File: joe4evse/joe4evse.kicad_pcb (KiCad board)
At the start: 2 copper layers, 100 x 100 mm, 77 parts, among them J1 USB_B_Micro, J10 Conn_01x02, J11 Conn_01x02, J2 Conn_01x03, J3 Conn_01x03, J4 Conn_01x02, J5 Conn_01x03, J6 CONNFLY_Elec_DS1129-04-S8B0P-X, J7 8P8C_LED_Shielded, J8 Conn_01x02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

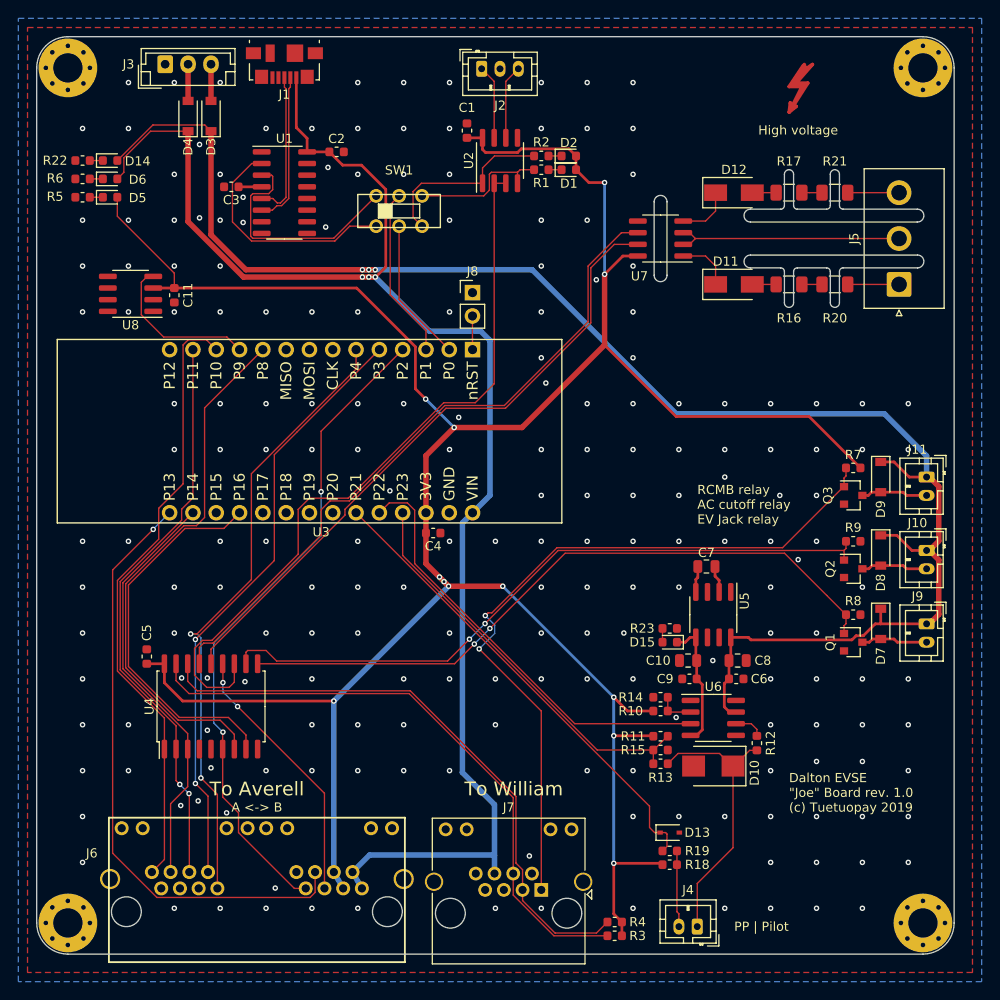
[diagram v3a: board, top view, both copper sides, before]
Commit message: joe/*: Add 0.1" header for easy access to RJ45 signals
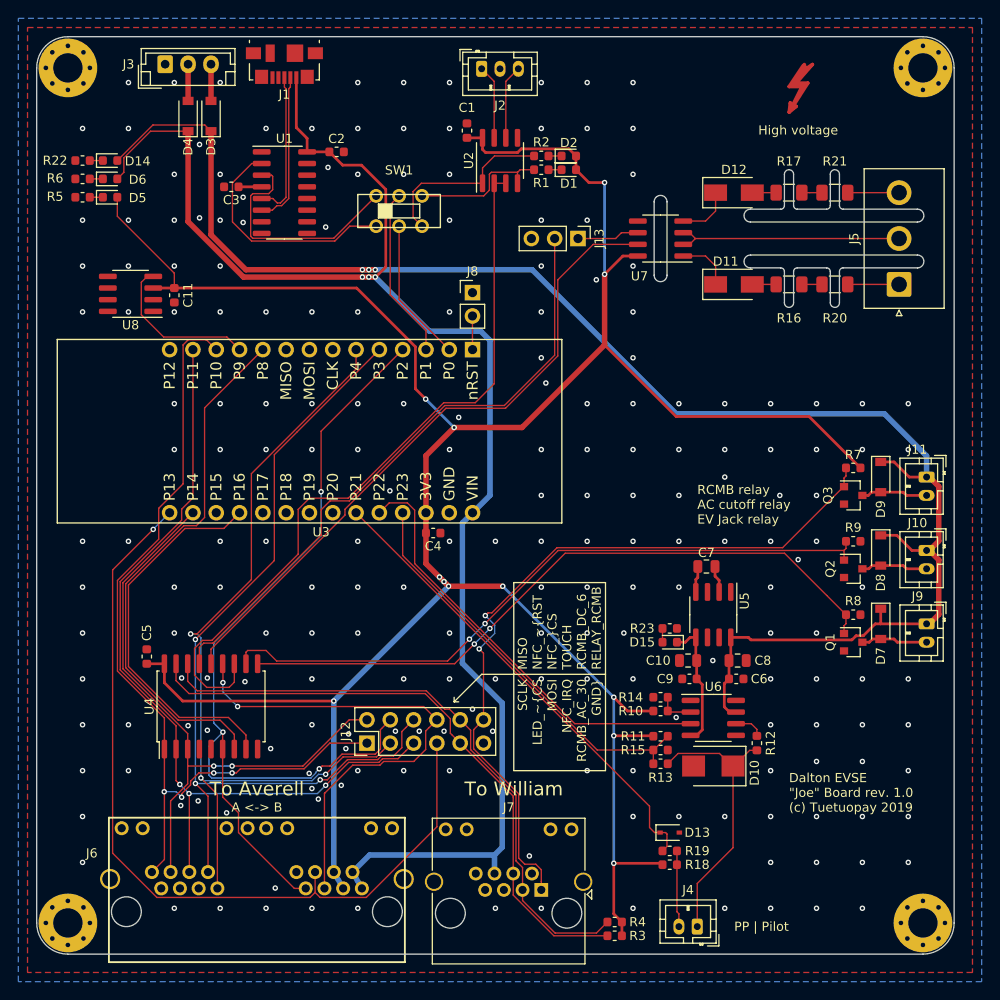
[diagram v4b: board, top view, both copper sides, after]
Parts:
- added J12: Conn_02x06_Odd_Even, Connector_PinHeader_2.54mm:PinHeader_2x06_P2.54mm_Vertical, F.Cu at (136.0, 127.0)
- added J13: Conn_01x03, Connector_PinHeader_2.54mm:PinHeader_1x03_P2.54mm_Vertical, F.Cu at (159.0, 72.0)
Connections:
- net /fipy/RCMB_AC_30mA renamed /RCMB_AC_30
- net /fipy/RCMB_DC_6mA renamed /RCMB_DC_6
- U4 pad 15: /evse/AC_TEST1 -> Net-(J13-Pad2)
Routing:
- net Net-(J13-Pad2): track 0.00 -> 68.0 mm
- net /evse/AC_TEST1: track 73.5 -> 6.79 mm
- net /NFC_~RST: track 72.2 -> 101.3 mm, vias 2 -> 3
- net /NFC_~CS: track 65.8 -> 93.5 mm, vias 2 -> 3
- net /MOSI: track 63.4 -> 90.1 mm, vias 2 -> 3
- net /NFC_IRQ: track 66.2 -> 92.0 mm
- net /TOUCH: track 29.1 -> 54.8 mm
- net /SCLK: track 67.4 -> 92.7 mm, vias 0 -> 4
- net /LED_~CS: track 68.2 -> 90.7 mm, vias 2 -> 3
- net /MISO: track 46.0 -> 67.7 mm, vias 0 -> 2
- net /RELAY_RCMB: track 80.9 -> 82.5 mm
- net /evse/AC_TEST0: track 70.3 -> 71.6 mm
- net /RCMB_DC_6: track 65.7 -> 67.1 mm
- net /RCMB_AC_30: track 66.6 -> 67.6 mm
- net +5V: track 167.6 -> 168.3 mm
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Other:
- board text added: "MISO NFC_~RST NFC_~CS TOUCH RCMB_DC_6 RELAY_RCMB"
- board text added: "SCLK LED_~CS MOSI NFC_IRQ RCMB_AC_30 GND"

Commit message: joe/pcb: Misc silk fixes
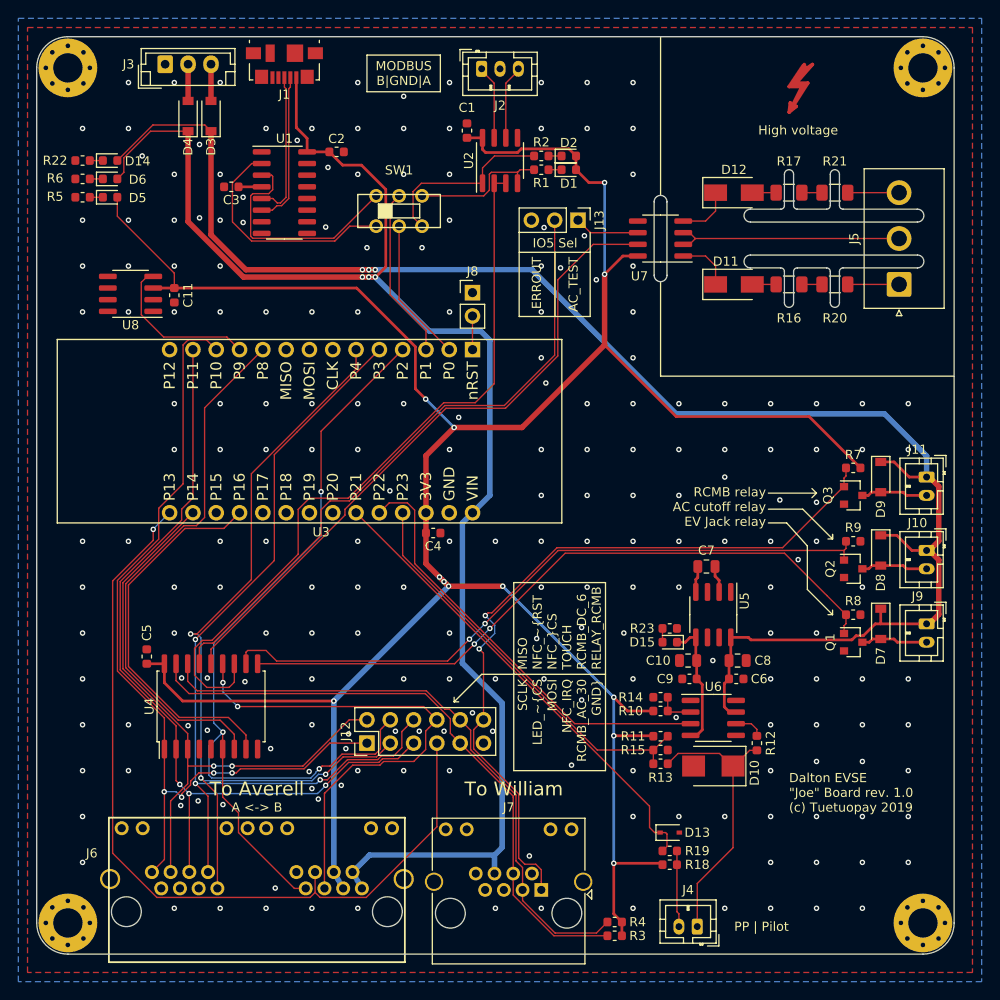
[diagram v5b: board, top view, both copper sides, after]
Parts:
- moved J13 2.00 mm to (159.0, 70.0)
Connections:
- net Net-(J2-Pad1) renamed /MOD_B
- net Net-(J2-Pad3) renamed /MOD_A
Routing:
- net Net-(J13-Pad2): track 68.0 -> 70.0 mm
- net GND: vias 212 -> 217
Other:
- board text added: "AC_TEST"
- board text added: "ERROUT"
- board text added: "IO5 Sel"
- board text added: "MODBUS B|GND|A"

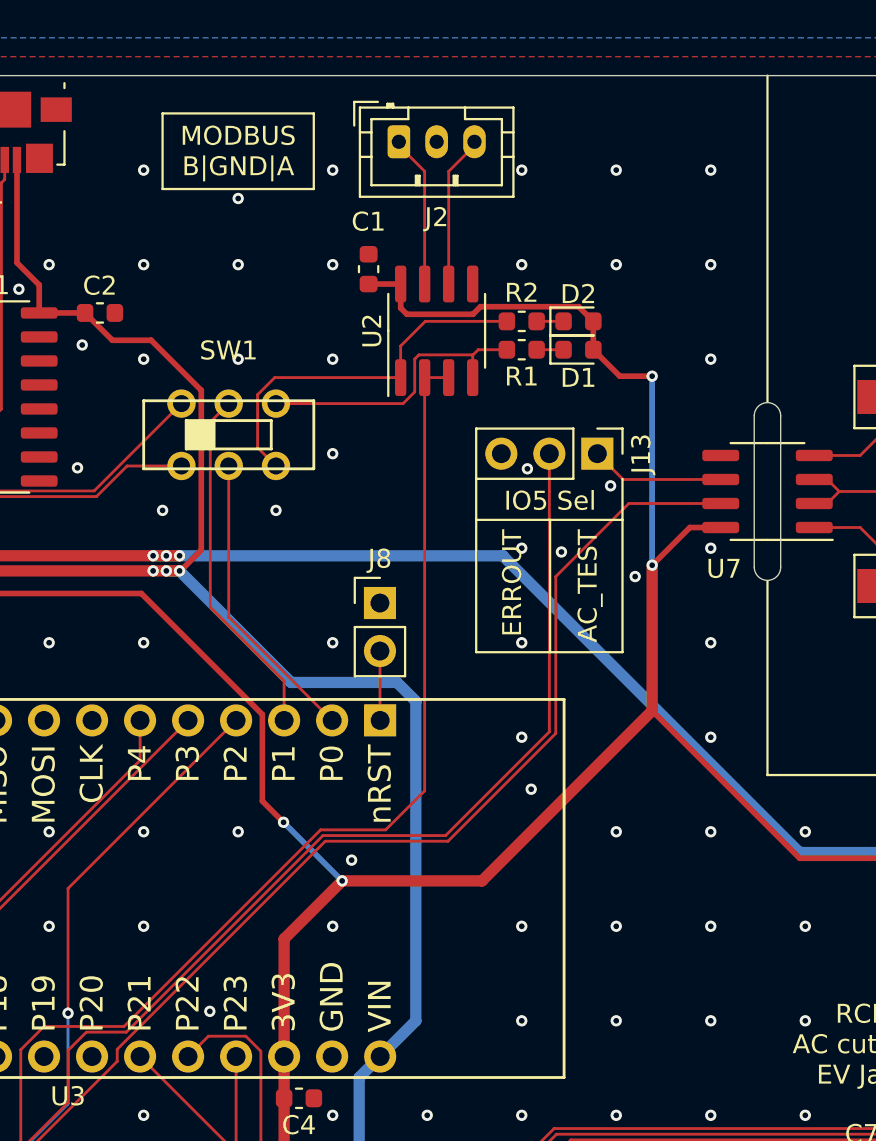
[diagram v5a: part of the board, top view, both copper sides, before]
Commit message: joe: Add 12V ERROUT
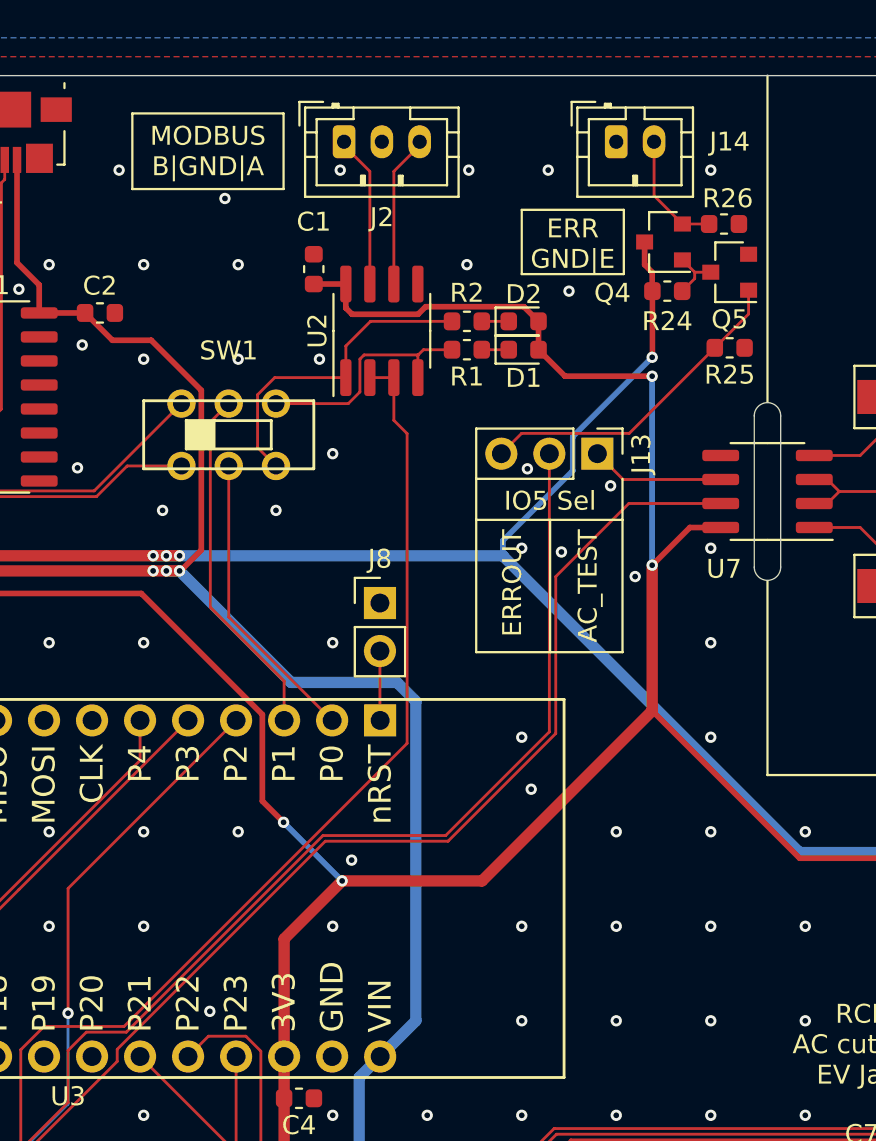
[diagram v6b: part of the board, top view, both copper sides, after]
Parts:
- added J14: Conn_01x02, Connector_JST:JST_PH_B2B-PH-K_1x02_P2.00mm_Vertical, F.Cu at (160.0, 53.5)
- added Q4: AO3401A, Package_TO_SOT_SMD:SOT-23, F.Cu at (162.5, 58.8)
- added Q5: AO3402, Package_TO_SOT_SMD:SOT-23, F.Cu at (166.0, 60.4)
- added R24: 10k, Resistor_SMD:R_0603_1608Metric, F.Cu at (162.7, 61.4)
- added R25: 10k, Resistor_SMD:R_0603_1608Metric, F.Cu at (166.0, 64.4)
- added R26: 10k, Resistor_SMD:R_0603_1608Metric, F.Cu at (165.7, 57.9)
- moved C1 2.90 mm to (144.0, 60.2)
- moved D1 2.90 mm to (155.1, 64.5)
- moved D2 2.90 mm to (155.1, 63.0)
- moved J2 2.90 mm to (145.6, 53.5)
- moved R1 2.90 mm to (152.1, 64.5)
- moved R2 2.90 mm to (152.1, 63.0)
- moved U2 2.90 mm to (147.6, 63.5)
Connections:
- J13 pad 3: /fipy/ERROUT -> /fipy/ERR
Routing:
- net +12V: track 178.3 -> 198.3 mm, vias 3 -> 4
- net /fipy/ERR: track 0.00 -> 17.4 mm
- net /fipy/ERROUT: track 0.00 -> 6.38 mm
- net Net-(Q4-Pad1): track 0.00 -> 3.04 mm
- net /MOD_TX: track 19.9 -> 17.0 mm
- net /MOD_RX: track 15.6 -> 12.7 mm
- net +3V3: track 295.6 -> 298.5 mm
- net /MOD_EN: track 80.6 -> 78.5 mm
- net GND: vias 217 -> 213
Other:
- board text added: "ERR GND|E"

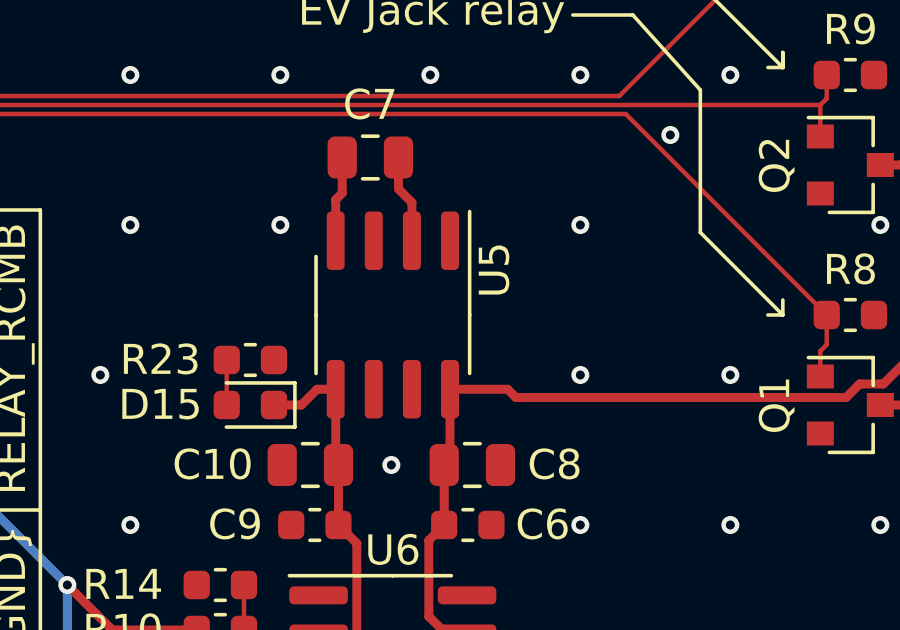
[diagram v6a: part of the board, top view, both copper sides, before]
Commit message: joe/*: Connect charge pump boost pin to +12V
This increases the switching frequency from 10kHz to 45kHz, making the
pump capacitor resonating inaudible.
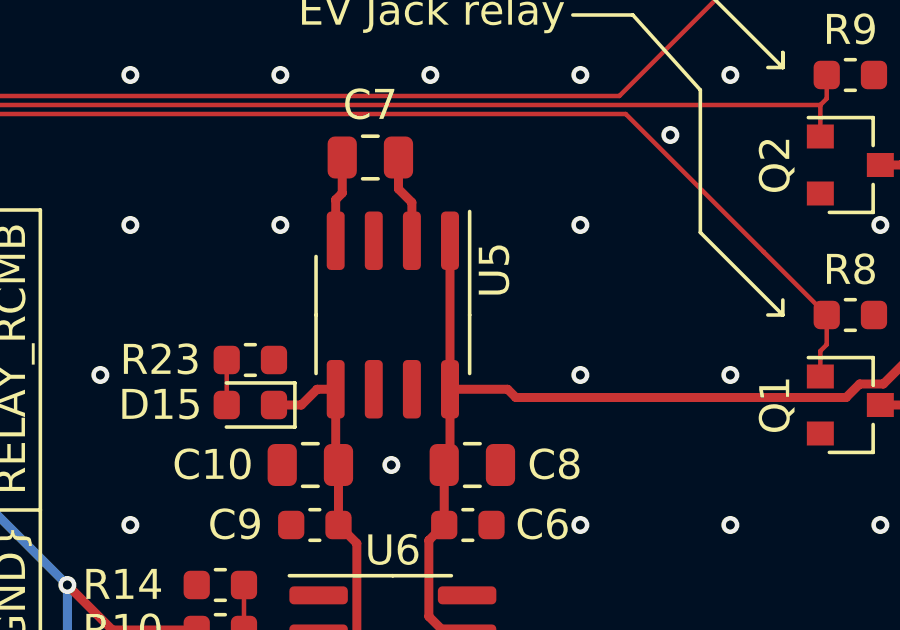
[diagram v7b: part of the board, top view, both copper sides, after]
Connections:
- U5 pad 1: Net-(U5-Pad1) -> +12V
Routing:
- net +12V: track 198.3 -> 203.3 mm

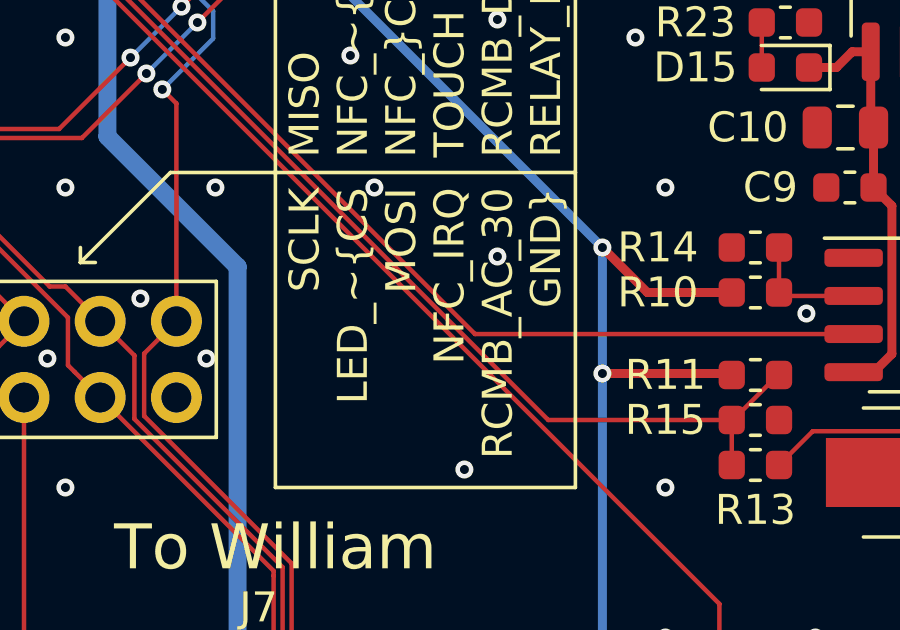
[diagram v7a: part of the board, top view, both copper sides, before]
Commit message: joe/*: Rename LED_CS signal to LED_LAT
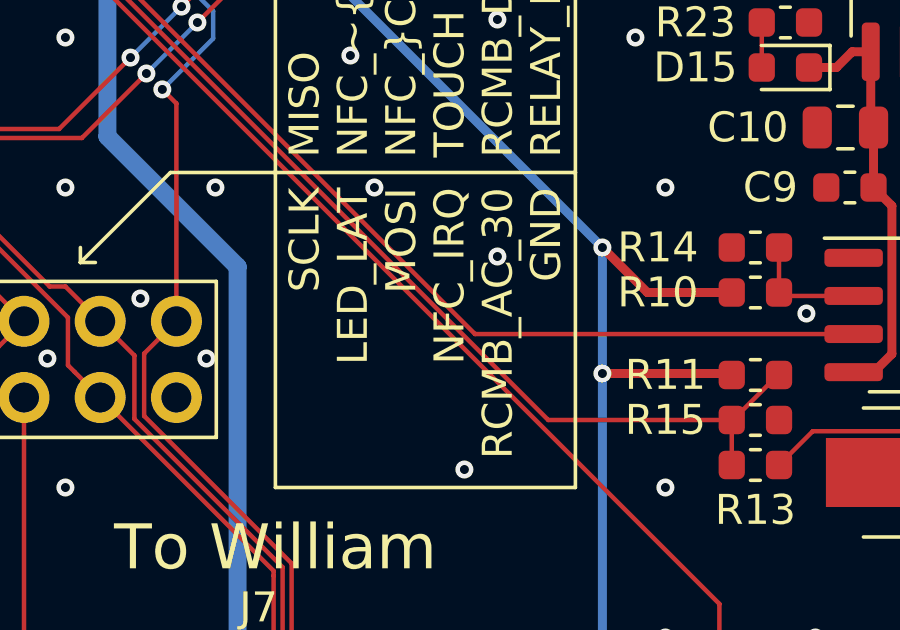
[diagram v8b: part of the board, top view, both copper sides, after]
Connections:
- net /LED_~CS renamed /LED_LAT
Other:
- board text added: "SCLK LED_LAT MOSI NFC_IRQ RCMB_AC_30 GND"
- board text removed: "SCLK LED_~CS MOSI NFC_IRQ RCMB_AC_30 GND"
